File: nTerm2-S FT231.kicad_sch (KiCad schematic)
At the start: 127 parts, among them J1 VGA, J2 Keyboard, J3 Mouse, J4 Line-out/Speaker, J5 RS-232 V.24, J6 USB_C_Receptacle_USB2.0_16P, J7 Line-out/Speaker, J8 10K pot, K1 IM41 3V, K2 IM41 3V, K3 IM41 3V, Q1 BC817, Q2 BC817, Q3 BC817, Q4 BC817, Q5 BC817, Q6 BC817, Q7 BC817, Q8 BC817, SW1 IO0, SW2 RESET, SW3 DEFAULTS, U1 ESP32-WROOM-32, U2 LM386, U3 MAX3232E, U4 DS2417, U5 NCP1117-3.3_SOT223, U6 USBLC6-2SC6, U7 FT231XS, Y1 32.768MHz

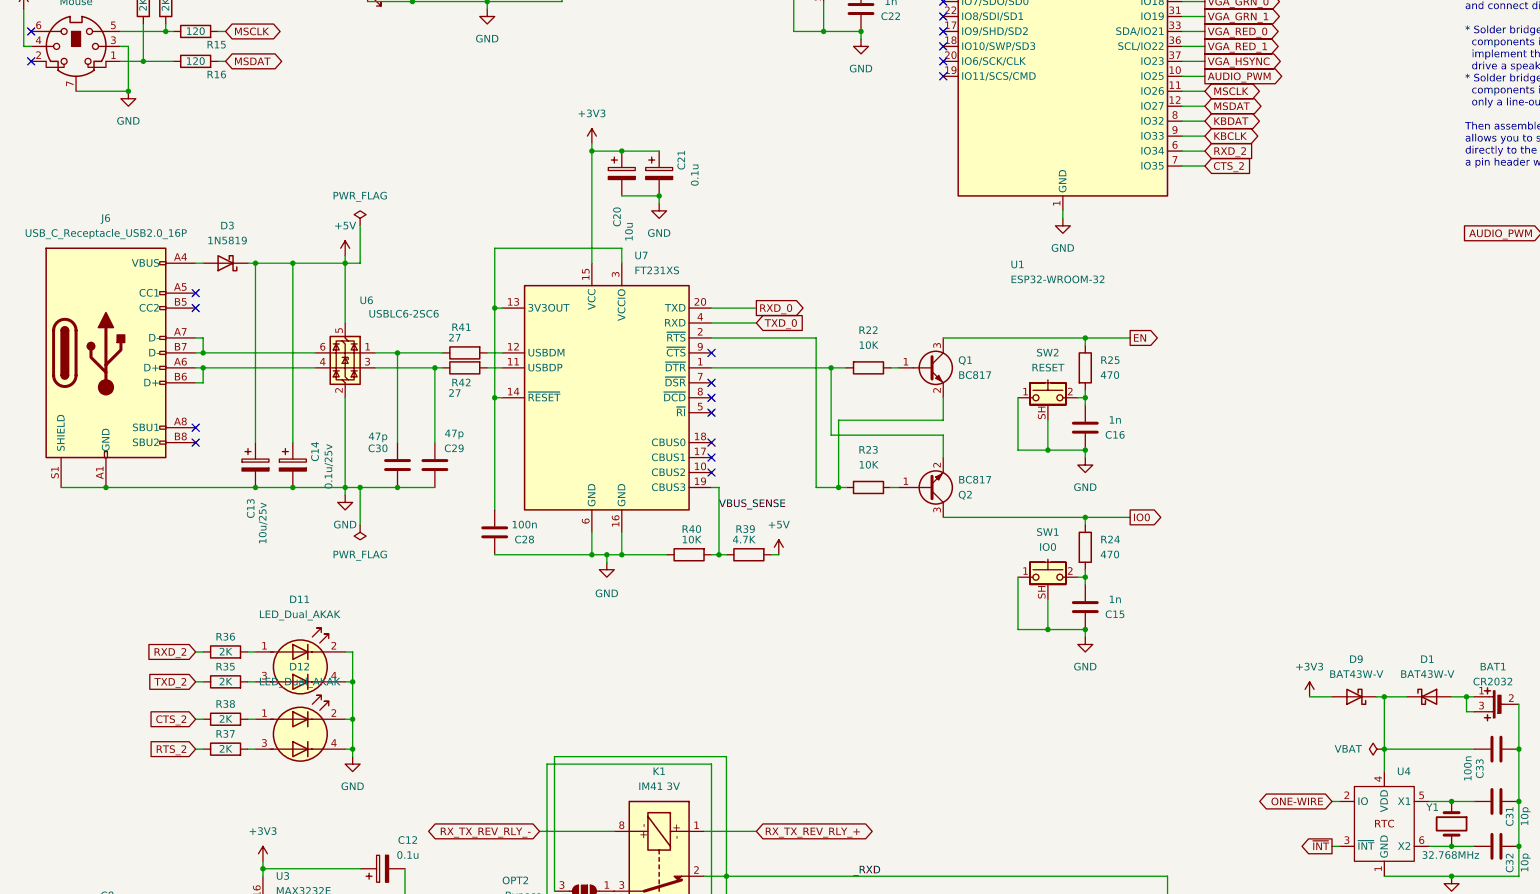
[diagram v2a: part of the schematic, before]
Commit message: Big booboo! I forgot about the 5K1 resistors necessary on the CC lines of the USB-C connector. With those, the USB-C will not give power to the board. If you use a USB-A to USB-C cable, it works great. And that's what I've been doing for months. So I never noticed that it didn't work with USB-C to USB-C. I remember making a mental note about it at some time, but I never did add them. So we need a V0.12 to fix that. - Added the 5K1 resistors for the CC lines of the USB-C connector. - Refactored the placement and routing around the USBLC6-2SC6 to make room for the two 5K1 resistors. - Refactored the 3V3 power distribution to the FT231 and the ESP32. - Changed the position of the silkscreen texts. Added the URLs to all the repositories. Made a big logo on the back of the PCB now. - Revision 0.12 - Generated gerbers and drill files. - Updated the images.
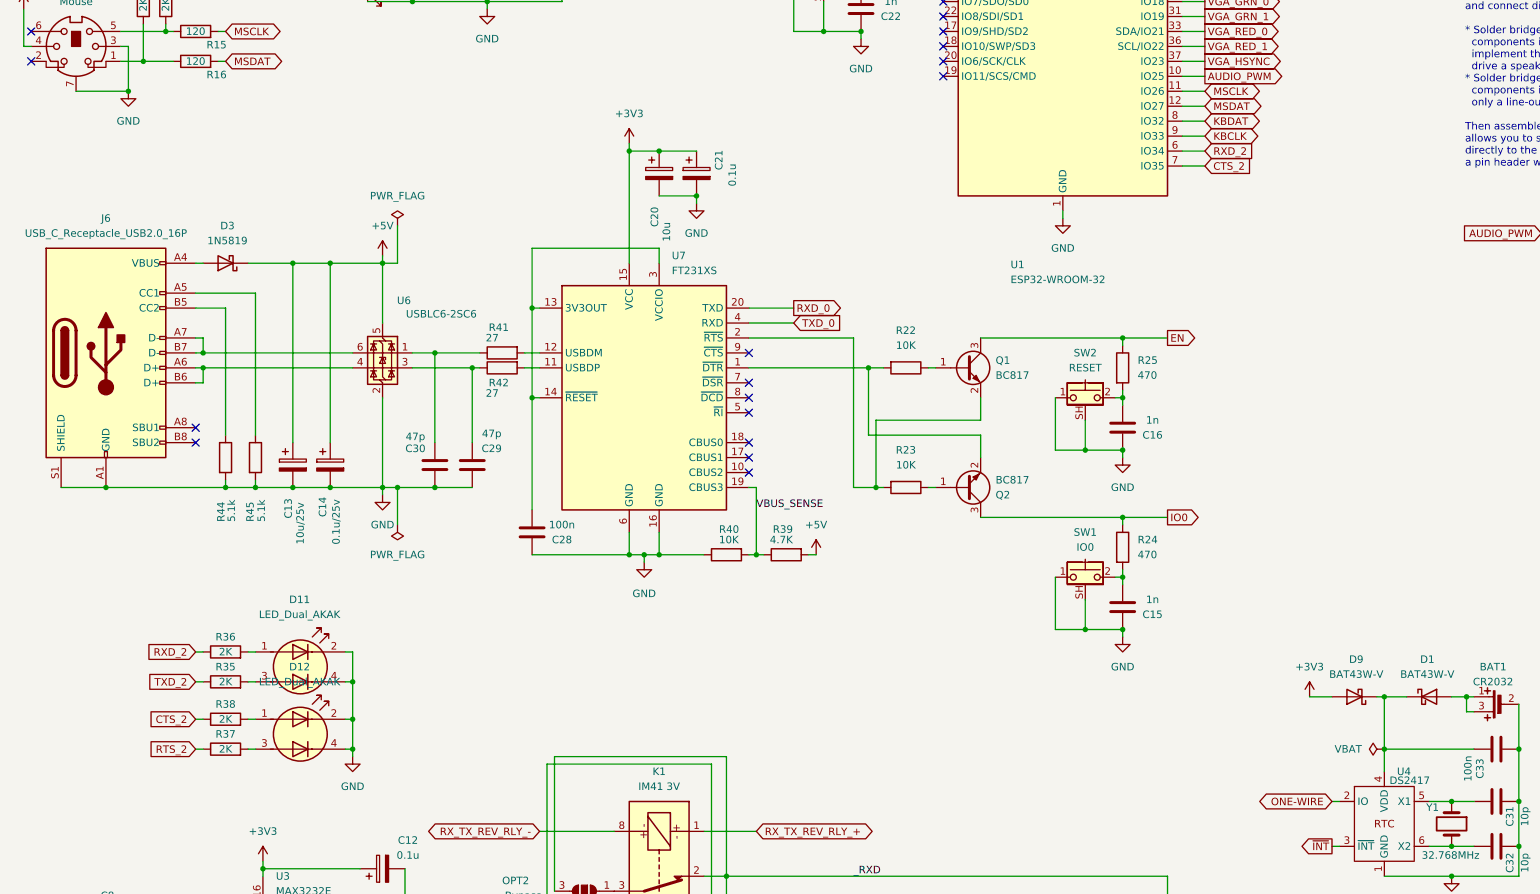
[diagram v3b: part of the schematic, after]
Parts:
- added R44, R45: 5.1k, nTerm2-S:R_0603_1608Metric_Pad0.98x0.95mm_HandSolder, symbol nTerm2-S:R
- U4: footprint nTerm2-S:TSOC-6_3.76x3.94mm_P1.27mm -> nTerm2-S:TSOC-6_3.76x3.94mm_P1.27mm_handsolder
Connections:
- net GND: now also R44.2, R45.2
- net at J6.A5 (CC1): now also R45.1
- net at J6.B5 (CC2): now also R44.1
- no-connect marks 32 -> 30
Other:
- moved on the sheet: C13, C14, C15, C16, C20, C21, C28, C29, C30, Q1, Q2, R22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
